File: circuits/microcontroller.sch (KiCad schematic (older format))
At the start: 17 parts, among them U13 ESP32-WROOM-32, U14 Si7020-A20

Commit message: Sent to fab.
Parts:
- removed C23: C_0.1uF, Capacitor_SMD:C_0603_1608Metric_Pad1.08x0.95mm_HandSolder, symbol Open_Automation:C_0.1uF
- removed D12: LED_G, Diode_SMD:D_0603_1608Metric_Pad1.05x0.95mm_HandSolder, symbol Open_Automation:LED_G
- removed R75, R76, R77, R78: R_10K, Resistor_SMD:R_0603_1608Metric_Pad0.98x0.95mm_HandSolder, symbol Open_Automation:R_10K
- removed U14: Si7020-A20, Package_DFN_QFN:DFN-6-1EP_3x3mm_P1mm_EP1.5x2.4mm, symbol Sensor_Humidity:Si7020-A20
- added D10: LED_G, Diode_SMD:D_0603_1608Metric_Pad1.05x0.95mm_HandSolder, symbol Open_Automation:LED_G
- added R1: R_10K, Resistor_SMD:R_0603_1608Metric_Pad0.98x0.95mm_HandSolder, symbol Open_Automation:R_10K
- renumbered C21 to C30, C22 to C31, D10 to D8, D11 to D9, R73 to R63, R74 to R64
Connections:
- net labels added: IO12, IO14, IO21, IO22
- net labels removed: SCL, SDA
- wire segments 82 -> 72
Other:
- moved on the sheet: C30, C31, D8, D9, EN1, PROG1, R63, R64, U13

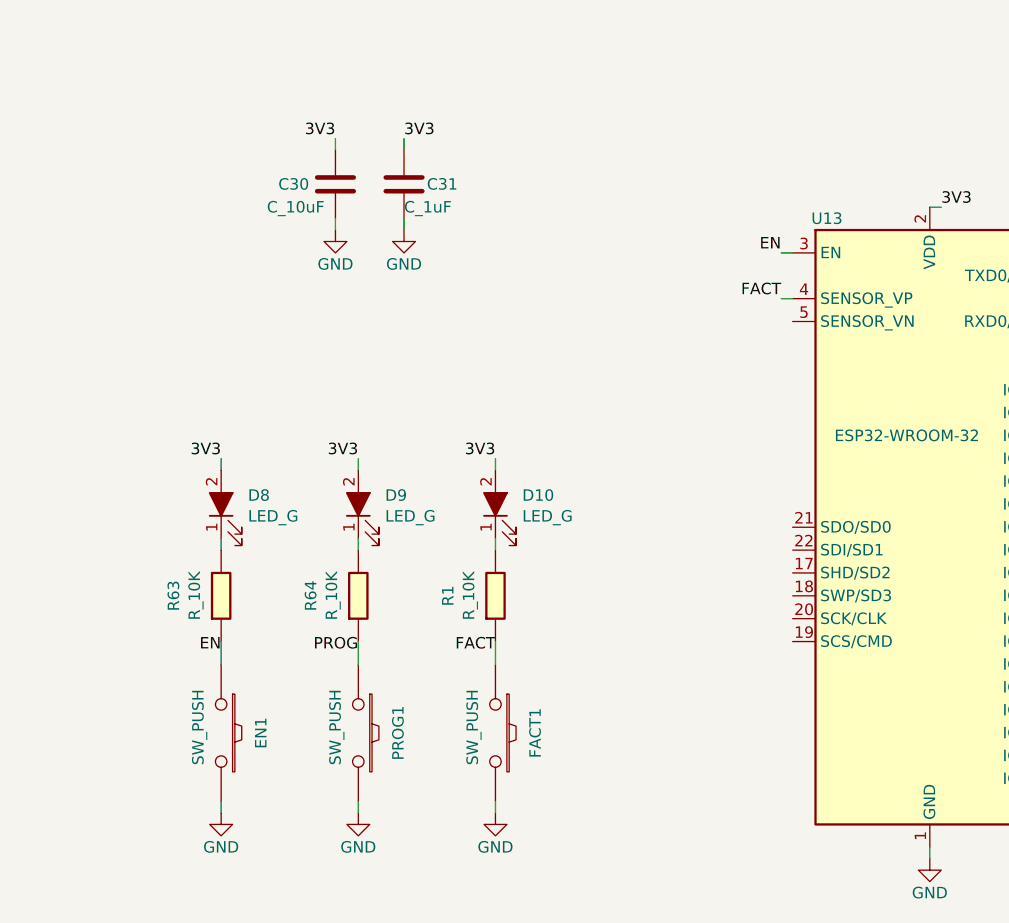
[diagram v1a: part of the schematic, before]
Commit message: finished schematic corrections, working on layout
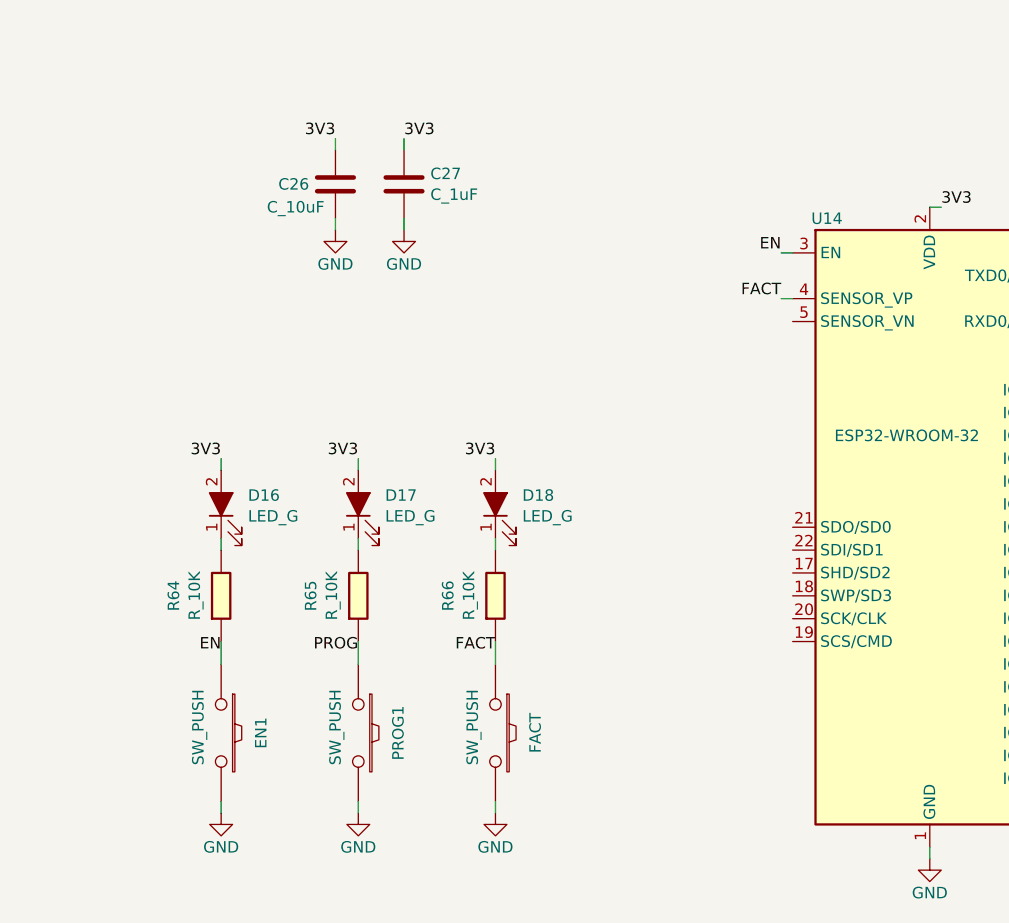
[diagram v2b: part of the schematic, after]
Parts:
- removed C31: C_1uF, Capacitor_SMD:C_0603_1608Metric_Pad1.08x0.95mm_HandSolder, symbol Open_Automation:C_1uF
- added C27: C_1uF, Capacitor_SMD:C_0603_1608Metric_Pad1.08x0.95mm_HandSolder, symbol Open_Automation:C_1uF
- renumbered C30 to C26, D8 to D16, D9 to D17, D10 to D18, FACT1 to FACT, R63 to R64, R64 to R65, R1 to R66, U13 to U14
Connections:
- net 3V3: now also C27.1
- net GND: now also C27.2
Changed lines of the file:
@@
 $Descr USLetter 11000 8500
 encoding utf-8
-Sheet 12 12
+Sheet 11 12
 Title ""
 Date ""
@@
 P 4200 4150
 AR Path="/5A7BADDB/5CC2D1AD" Ref="R?"  Part="1"
-AR Path="/6077D777/5CC2D1AD" Ref="R64"  Part="1"
-F 0 "R64" V 3993 4150 50  0000 C CNN
+AR Path="/6077D777/5CC2D1AD" Ref="R65"  Part="1"
+F 0 "R65" V 3993 4150 50  0000 C CNN
 F 1 "R_10K" V 4084 4150 50  0000 C CNN
 F 2 "Resistor_SMD:R_0603_1608Metric_Pad0.98x0.95mm_HandSolder" V 4130 4150 50  0001 C CNN
@@
 P 3600 4150
 AR Path="/5A7BADDB/5CC2EC19" Ref="R?"  Part="1"
-AR Path="/6077D777/5CC2EC19" Ref="R63"  Part="1"
-F 0 "R63" V 3393 4150 50  0000 C CNN
+AR Path="/6077D777/5CC2EC19" Ref="R64"  Part="1"
+F 0 "R64" V 3393 4150 50  0000 C CNN
 F 1 "R_10K" V 3484 4150 50  0000 C CNN
 F 2 "Resistor_SMD:R_0603_1608Metric_Pad0.98x0.95mm_HandSolder" V 3530 4150 50  0001 C CNN
@@
 P 3600 3750
 AR Path="/5A7BADDB/5CC255BE" Ref="D?"  Part="1"
-AR Path="/6077D777/5CC255BE" Ref="D8"  Part="1"
-F 0 "D8" V 3639 3633 50  0000 R CNN
+AR Path="/6077D777/5CC255BE" Ref="D16"  Part="1"
+F 0 "D16" V 3639 3633 50  0000 R CNN
 F 1 "LED_G" V 3548 3633 50  0000 R CNN
 F 2 "Diode_SMD:D_0603_1608Metric_Pad1.05x0.95mm_HandSolder" H 3600 3750 50  0001 C CNN
@@
 P 4200 3750
 AR Path="/5A7BADDB/5CC26ACF" Ref="D?"  Part="1"
-AR Path="/6077D777/5CC26ACF" Ref="D9"  Part="1"
-F 0 "D9" V 4239 3633 50  0000 R CNN
+AR Path="/6077D777/5CC26ACF" Ref="D17"  Part="1"
+F 0 "D17" V 4239 3633 50  0000 R CNN
 F 1 "LED_G" V 4148 3633 50  0000 R CNN
 F 2 "Diode_SMD:D_0603_1608Metric_Pad1.05x0.95mm_HandSolder" H 4200 3750 50  0001 C CNN
@@
 P 3600 5100
 AR Path="/5A7BADDB/601E8A98" Ref="#PWR?"  Part="1"
-AR Path="/6077D777/601E8A98" Ref="#PWR097"  Part="1"
-F 0 "#PWR097" H 3600 4850 50  0001 C CNN
+AR Path="/6077D777/601E8A98" Ref="#PWR099"  Part="1"
+F 0 "#PWR099" H 3600 4850 50  0001 C CNN
 F 1 "GND" H 3600 4950 50  0000 C CNN
 F 2 "" H 3600 5100 50  0000 C CNN
@@
 P 4200 5100
 AR Path="/5A7BADDB/601E9002" Ref="#PWR?"  Part="1"
-AR Path="/6077D777/601E9002" Ref="#PWR099"  Part="1"
-F 0 "#PWR099" H 4200 4850 50  0001 C CNN
+AR Path="/6077D777/601E9002" Ref="#PWR0101"  Part="1"
+F 0 "#PWR0101" H 4200 4850 50  0001 C CNN
 F 1 "GND" H 4200 4950 50  0000 C CNN
 F 2 "" H 4200 5100 50  0000 C CNN
@@
 $EndComp
 $Comp
-L Open_Automation:C_1uF C?
-U 1 1 5B2CA474
-P 4400 2350
-AR Path="/5A7BADDB/5B2CA474" Ref="C?"  Part="1"
-AR Path="/6077D777/5B2CA474" Ref="C31"  Part="1"
-F 0 "C31" H 4500 2350 50  0000 L CNN
-F 1 "C_1uF" H 4400 2250 50  0000 L CNN
-F 2 "Capacitor_SMD:C_0603_1608Metric_Pad1.08x0.95mm_HandSolder" H 4500 2650 50  0001 C CNN
-F 3 "https://datasheet.lcsc.com/szlcsc/Samsung-Electro-Mechanics-CL10A106MA8NRNC_C96446.pdf" H 4400 2100 50  0001 C CNN
-F 4 "CL10A106MA8NRNC" H 4525 2550 60  0001 C CNN "Part Number"
-F 5 "C96446" H 450 400 50  0001 C CNN "LCSC"
-	1    4400 2350
-	1    0    0    -1
-$EndComp
-$Comp
 L Open_Automation:C_10uF C?
 U 1 1 5B2706A8
 P 4100 2350
 AR Path="/5A7BADDB/5B2706A8" Ref="C?"  Part="1"
-AR Path="/6077D777/5B2706A8" Ref="C30"  Part="1"
-F 0 "C30" H 3850 2350 50  0000 L CNN
+AR Path="/6077D777/5B2706A8" Ref="C26"  Part="1"
+F 0 "C26" H 3850 2350 50  0000 L CNN
 F 1 "C_10uF" H 3800 2250 50  0000 L CNN
 F 2 "Capacitor_SMD:C_0603_1608Metric_Pad1.08x0.95mm_HandSolder" H 4200 2650 50  0001 C CNN
@@
 P 4400 2550
 AR Path="/5A7BADDB/5CC8C67A" Ref="#PWR?"  Part="1"
-AR Path="/6077D777/5CC8C67A" Ref="#PWR0100"  Part="1"
-F 0 "#PWR0100" H 4400 2300 50  0001 C CNN
+AR Path="/6077D777/5CC8C67A" Ref="#PWR0102"  Part="1"
+F 0 "#PWR0102" H 4400 2300 50  0001 C CNN
 F 1 "GND" H 4400 2400 50  0000 C CNN
 F 2 "" H 4400 2550 50  0000 C CNN
@@
 P 4100 2550
 AR Path="/5A7BADDB/5CC8CF13" Ref="#PWR?"  Part="1"
-AR Path="/6077D777/5CC8CF13" Ref="#PWR098"  Part="1"
-F 0 "#PWR098" H 4100 2300 50  0001 C CNN
+AR Path="/6077D777/5CC8CF13" Ref="#PWR0100"  Part="1"
+F 0 "#PWR0100" H 4100 2300 50  0001 C CNN
 F 1 "GND" H 4100 2400 50  0000 C CNN
 F 2 "" H 4100 2550 50  0000 C CNN
@@
 P 6700 5300
 AR Path="/5A7BADDB/601D8E89" Ref="#PWR?"  Part="1"
-AR Path="/6077D777/601D8E89" Ref="#PWR0101"  Part="1"
-F 0 "#PWR0101" H 6700 5050 50  0001 C CNN
+AR Path="/6077D777/601D8E89" Ref="#PWR0104"  Part="1"
+F 0 "#PWR0104" H 6700 5050 50  0001 C CNN
 F 1 "GND" H 6700 5150 50  0000 C CNN
 F 2 "" H 6700 5300 50  0000 C CNN
@@
 $EndComp
 $Comp
-L Open_Automation:ESP32-WROOM-32 U13
+L Open_Automation:ESP32-WROOM-32 U14
 U 1 1 601C2110
 P 6700 3850
-F 0 "U13" H 6250 5200 50  0000 C CNN
+F 0 "U14" H 6250 5200 50  0000 C CNN
 F 1 "ESP32-WROOM-32" H 6600 4250 50  0000 C CNN
 F 2 "RF_Module:ESP32-WROOM-32" H 6700 2350 50  0001 C CNN
@@
 AR Path="/5ABD187E/5FF4AD17" Ref="PROG?"  Part="1"
 AR Path="/5A7BADDB/5FF4AD17" Ref="PROG?"  Part="1"
-AR Path="/6077D777/5FF4AD17" Ref="FACT1"  Part="1"
-F 0 "FACT1" H 4800 4925 50  0000 C CNN
+AR Path="/6077D777/5FF4AD17" Ref="FACT"  Part="1"
+F 0 "FACT" H 4800 4925 50  0000 C CNN
 F 1 "SW_PUSH" H 4775 4650 50  0000 C CNN
 F 2 "Button_Switch_SMD:SW_SPST_PTS645" H 4800 4750 50  0001 C CNN
@@
 P 4800 4150
 AR Path="/5A7BADDB/5FF4AD23" Ref="R?"  Part="1"
-AR Path="/6077D777/5FF4AD23" Ref="R1"  Part="1"
-F 0 "R1" V 4593 4150 50  0000 C CNN
+AR Path="/6077D777/5FF4AD23" Ref="R66"  Part="1"
+F 0 "R66" V 4593 4150 50  0000 C CNN
 F 1 "R_10K" V 4684 4150 50  0000 C CNN
 F 2 "Resistor_SMD:R_0603_1608Metric_Pad0.98x0.95mm_HandSolder" V 4730 4150 50  0001 C CNN
@@
 P 4800 3750
 AR Path="/5A7BADDB/5FF4AD2F" Ref="D?"  Part="1"
-AR Path="/6077D777/5FF4AD2F" Ref="D10"  Part="1"
-F 0 "D10" V 4839 3633 50  0000 R CNN
+AR Path="/6077D777/5FF4AD2F" Ref="D18"  Part="1"
+F 0 "D18" V 4839 3633 50  0000 R CNN
 F 1 "LED_G" V 4748 3633 50  0000 R CNN
 F 2 "Diode_SMD:D_0603_1608Metric_Pad1.05x0.95mm_HandSolder" H 4800 3750 50  0001 C CNN
@@
 P 4800 5100
 AR Path="/5A7BADDB/5FF4AD3A" Ref="#PWR?"  Part="1"
-AR Path="/6077D777/5FF4AD3A" Ref="#PWR0102"  Part="1"
-F 0 "#PWR0102" H 4800 4850 50  0001 C CNN
+AR Path="/6077D777/5FF4AD3A" Ref="#PWR0103"  Part="1"
+F 0 "#PWR0103" H 4800 4850 50  0001 C CNN
 F 1 "GND" H 4800 4950 50  0000 C CNN
 F 2 "" H 4800 5100 50  0000 C CNN
@@
 Wire Wire Line
 	6050 2850 6100 2850
+$Comp
+L Open_Automation:C_1uF C27
+U 1 1 61005386
+P 4400 2350
+F 0 "C27" H 4515 2396 50  0000 L CNN
+F 1 "C_1uF" H 4515 2305 50  0000 L CNN
+F 2 "Capacitor_SMD:C_0603_1608Metric_Pad1.08x0.95mm_HandSolder" H 4500 2650 50  0001 C CNN
+F 3 "https://datasheet.lcsc.com/szlcsc/Samsung-Electro-Mechanics-CL05A105KA5NQNC_C52923.pdf" H 4400 2100 50  0001 C CNN
+F 4 "C52923" H 4400 2750 50  0001 C CNN "LCSC"
+F 5 "CL05A105KA5NQNC" H 4525 2550 60  0001 C CNN "Part Number"
+	1    4400 2350
+	1    0    0    -1
+$EndComp
 $EndSCHEMATC

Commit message: finished layout, sent to board house
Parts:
- renumbered FACT to FACT1
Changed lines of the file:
@@
 AR Path="/5ABD187E/5FF4AD17" Ref="PROG?"  Part="1"
 AR Path="/5A7BADDB/5FF4AD17" Ref="PROG?"  Part="1"
-AR Path="/6077D777/5FF4AD17" Ref="FACT"  Part="1"
-F 0 "FACT" H 4800 4925 50  0000 C CNN
+AR Path="/6077D777/5FF4AD17" Ref="FACT1"  Part="1"
+F 0 "FACT1" H 4800 4925 50  0000 C CNN
 F 1 "SW_PUSH" H 4775 4650 50  0000 C CNN
 F 2 "Button_Switch_SMD:SW_SPST_PTS645" H 4800 4750 50  0001 C CNN
